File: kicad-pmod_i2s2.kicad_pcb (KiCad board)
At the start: 2 copper layers, 20.3 x 49.3 mm, 40 parts, among them J1 M/S, J2 pmod, J3 Audio Out, J4 Audio In, U1 74LVC1G126, U2 CS4344, U3 CS5343

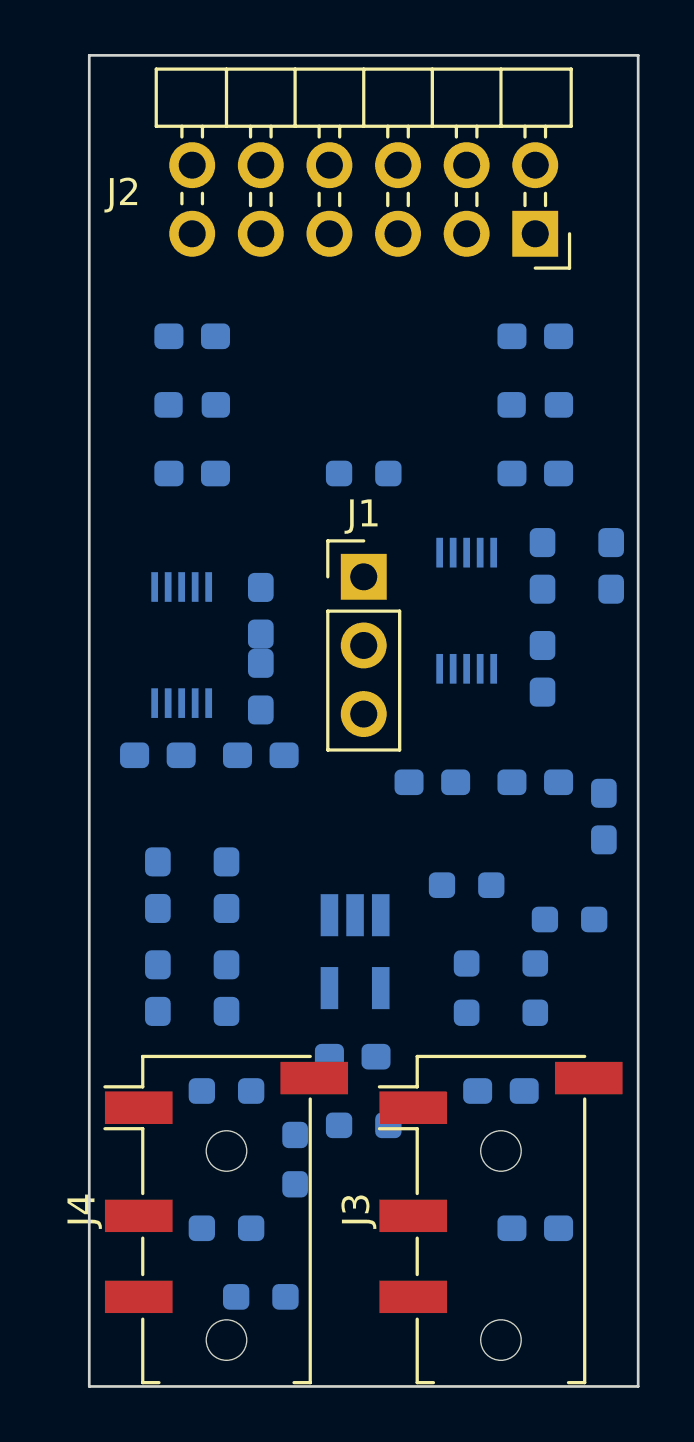
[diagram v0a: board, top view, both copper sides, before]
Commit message: finished placement and refdes arragement
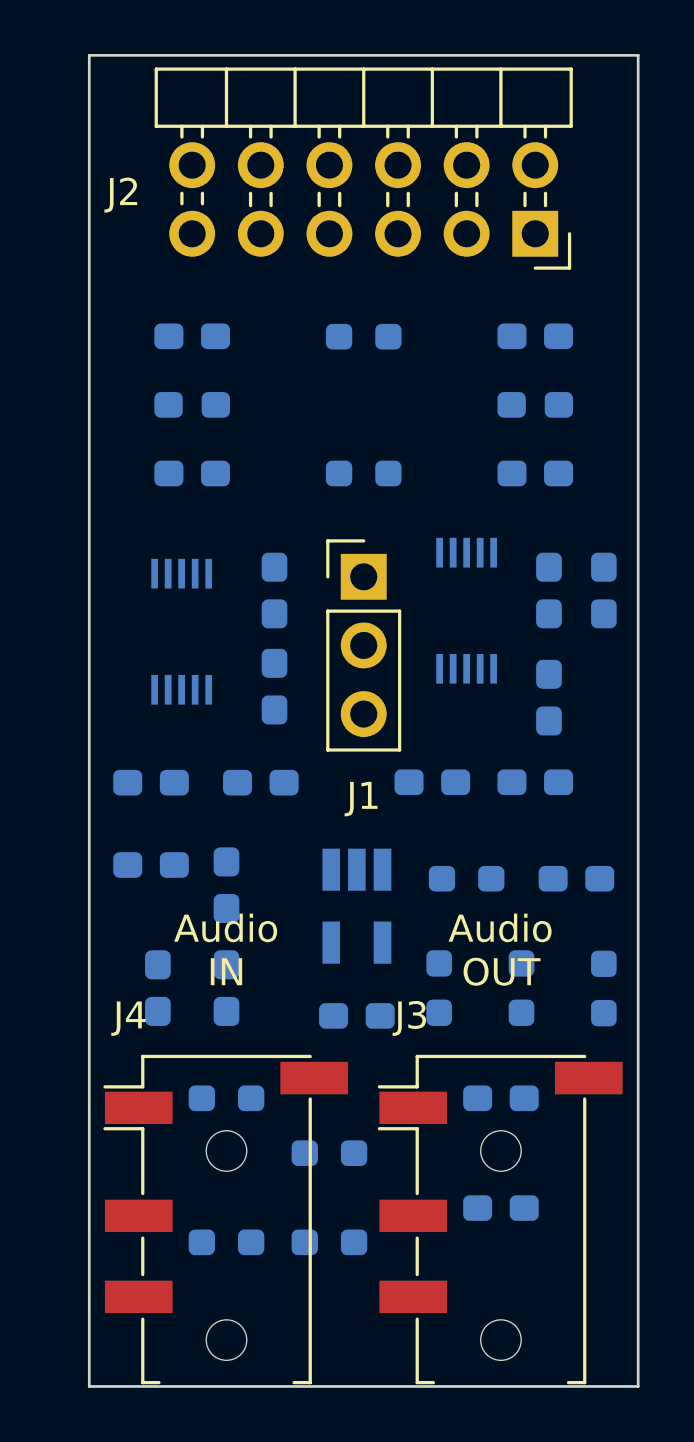
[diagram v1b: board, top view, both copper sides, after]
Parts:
- moved R1 29.2 mm to (120.7, 47.0)
- moved R8 3.24 mm to (119.4, 80.5)
- moved R3 2.85 mm to (129.5, 71.1), turned to -90 degrees
- moved C15 2.52 mm to (128.5, 67.1), turned to 0 degrees
- moved U1 1.68 mm to (120.4, 68.1)
- moved C1 1.52 mm to (120.4, 72.1)
- moved C20 1.47 mm to (125.7, 79.2)
- moved R7 1.29 mm to (119.4, 77.2), turned to 0 degrees
- moved C12 1.09 mm to (127.5, 60.4)
- moved C11 1.05 mm to (112.8, 63.5)
- moved R5 1.02 mm to (123.4, 71.1)
- moved C9 1.02 mm to (116.8, 63.5)
- moved C8 0.95 mm to (129.5, 56.4)
- moved C4 0.94 mm to (127.5, 56.4)
- moved C13 0.90 mm to (117.3, 56.4)
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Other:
- board text added: "Audio IN"
- board text added: "Audio OUT"

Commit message: 1.0 - jlcpcb order
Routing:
- net GND: track 0.00 -> 214.1 mm, vias 0 -> 26
- net +3V3: track 0.00 -> 48.7 mm, vias 0 -> 1
- net Net-(U2-VA): track 0.00 -> 42.3 mm
- net /SDOUT: track 0.00 -> 37.1 mm, vias 0 -> 2
- net /ADIN_MCLK: track 0.00 -> 32.3 mm, vias 0 -> 1
- net /ADIN_LRCLK: track 0.00 -> 29.2 mm, vias 0 -> 1
- net /ADIN_SCLK: track 0.00 -> 25.4 mm
- net Net-(R1-Pad1): track 0.00 -> 24.8 mm
- net Net-(U3-FILT+): track 0.00 -> 18.0 mm
- net Net-(U3-VA): track 0.00 -> 16.3 mm
- net /ADOUT_SDIN: track 0.00 -> 14.0 mm
- net Net-(U2-AOUTL): track 0.00 -> 13.1 mm
- net /ADOUT_MCLK: track 0.00 -> 12.6 mm
- net /ADOUT_SCLK: track 0.00 -> 12.6 mm
- net Net-(C18-Pad2): track 0.00 -> 12.0 mm
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- added copper zone on B.Cu, net GND
- added copper zone on F.Cu, net GND
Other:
- outline, holes or cut-outs redrawn
- board text added: "+3V3"
- board text added: "CS4344"
- board text added: "CS5343"
- board text added: "GND"
- board text added: "Master"
- board text added: "PMOD-I2S2 1.0 S59MZ"
- board text added: "Slave"
- board text added: "i-"
- board text added: "i-lrclk"
- board text added: "i-mclk"
- board text added: "i-sclk"
- board text added: "i-sdout"
- board text added: "o-"
- board text added: "o-lrclk"
- board text added: "o-mclk"
- board text added: "o-sclk"
- board text added: "o-sdin"
- board text added: "↑"
